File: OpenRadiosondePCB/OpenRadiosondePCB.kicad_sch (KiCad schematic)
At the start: 0 parts

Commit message: update
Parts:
- added IC1: SI4468-A2A-IMR, CustomLibs:QFN50P400X400X90-21N, symbol SI4468-A2A-IMR:SI4468-A2A-IMR
- added U1: STM32L476RGTx, Package_QFP:LQFP-64_10x10mm_P0.5mm, symbol MCU_ST_STM32L4:STM32L476RGTx
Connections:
- new net: U1.18 (VSS), U1.31 (VSS), U1.47 (VSS), U1.63 (VSS)

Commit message: Schematics inital work
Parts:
- added C1: 10u, symbol Device:C
- added C2, C3, C4, C5: 100n, symbol Device:C
- added C6, C7: C, symbol Device:C
- added J1: Conn_01x05, Connector_PinHeader_2.54mm:PinHeader_1x05_P2.54mm_Vertical, symbol Connector_Generic:Conn_01x05
- added Y1: Crystal_GND23, symbol Device:Crystal_GND23
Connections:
- net +3V3: now reaches U1.1 (VBAT)
- net +3V3: now also U1.19 (VDD), U1.32 (VDD), U1.64 (VDD), C1.1, C2.1, C3.1, C4.1, J1.1 (Pin_1)
- net GND: now reaches U1.12 (VSSA)
- net GND: now also U1.18 (VSS), U1.31 (VSS), U1.47 (VSS), U1.63 (VSS), C1.2, C2.2, C3.2, C4.2, C5.2, C6.2, C7.2, J1.5 (Pin_5), Y1.2 (G), Y1.3 (G)
- net at U1.46 (PA13): now also J1.2 (Pin_2)
- net at U1.49 (PA14): now also J1.3 (Pin_3)
- net RST: now reaches U1.7 (NRST)
- net RST: now also C5.1, J1.4 (Pin_4)
- new net HSE_IN: C6.1, Y1.1
- new net HSE_OUT: C7.1, Y1.4
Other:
- note added: "1 - VCC 2 - SWDIO 3 - SWCLK 4 - RST 5 - GND"

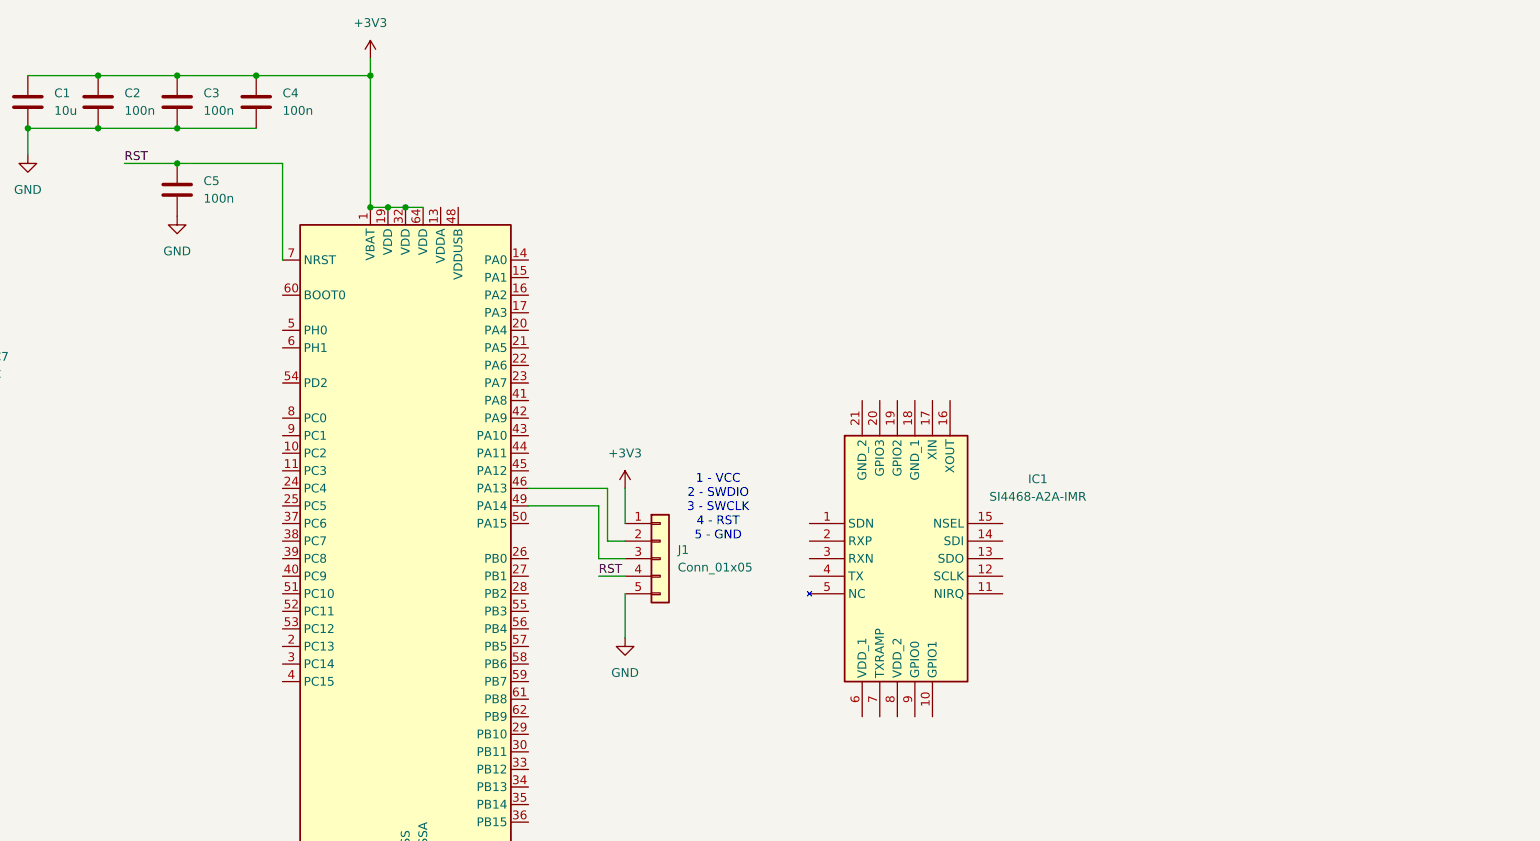
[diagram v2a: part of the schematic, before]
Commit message: Further PCB design and added CubeMX project
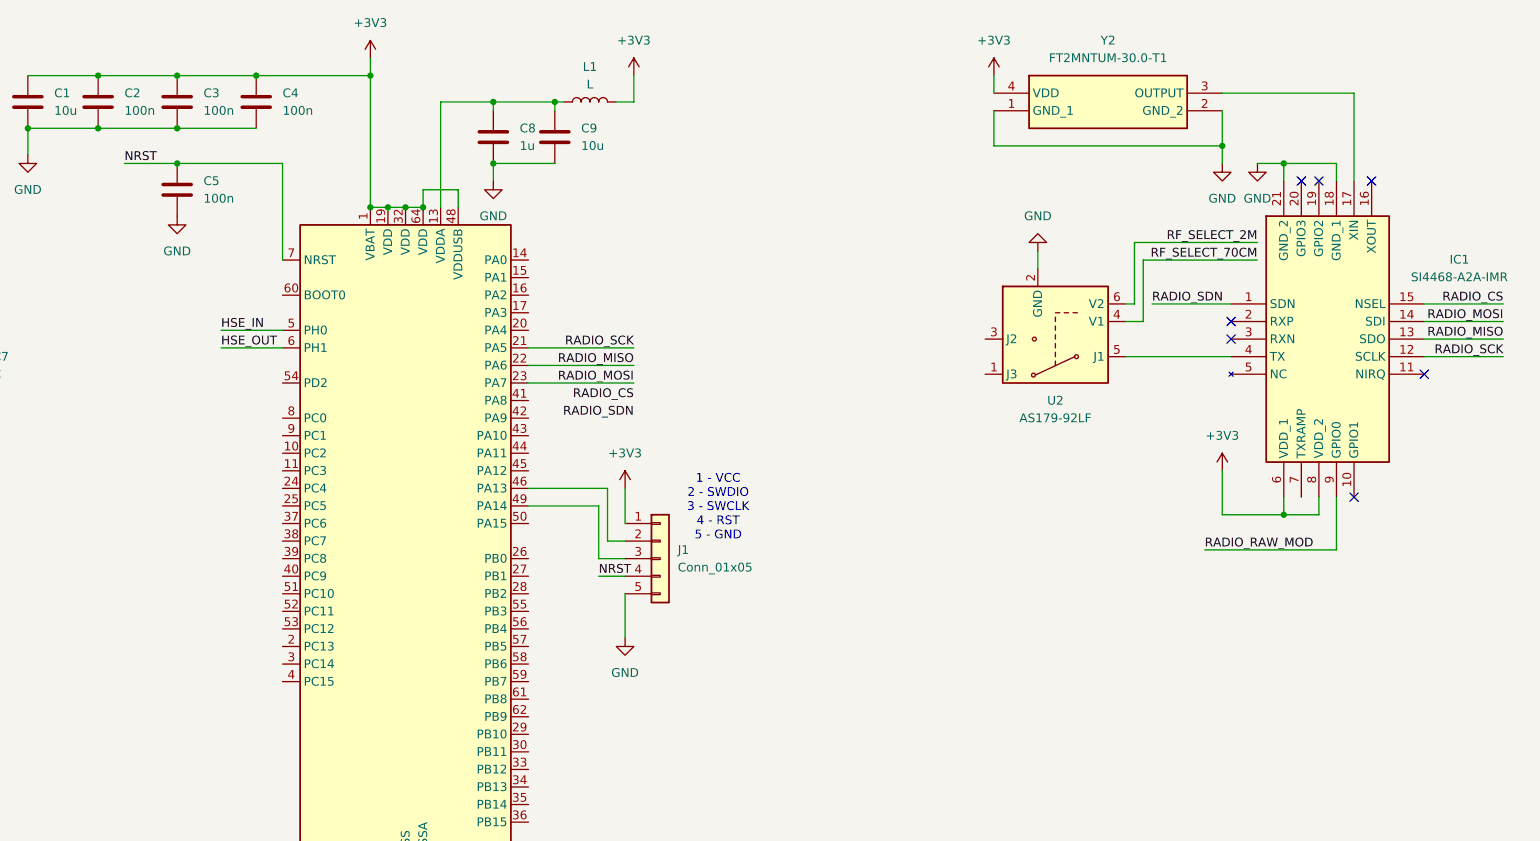
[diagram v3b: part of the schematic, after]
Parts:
- added C8: 1u, symbol Device:C
- added C9: 10u, symbol Device:C
- added L1: L, symbol Device:L
- added U2: AS179-92LF, Package_TO_SOT_SMD:SOT-363_SC-70-6, symbol RF_Switch:AS179-92LF
- added Y2: FT2MNTUM-30.0-T1, FT2MNTUM300T1, symbol FT2MNTUM-30_0-T1:FT2MNTUM-30.0-T1
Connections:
- net +3V3: now also IC1.6 (VDD_1), IC1.8 (VDD_2), U1.48 (VDDUSB), L1.2, Y2.4 (VDD)
- net GND: now also IC1.18 (GND_1), IC1.21 (GND_2), C8.2, C9.2, U2.2 (GND), Y2.1 (GND_1), Y2.2 (GND_2)
- net HSE_IN: now also U1.5 (PH0)
- net HSE_OUT: now also U1.6 (PH1)
- net RADIO_SDN: now reaches IC1.1 (SDN)
- net RADIO_SCK: now reaches IC1.12 (SCLK)
- net RADIO_SCK: now also U1.21 (PA5)
- net RADIO_MISO: now reaches IC1.13 (SDO)
- net RADIO_MISO: now also U1.22 (PA6)
- net RADIO_MOSI: now reaches IC1.14 (SDI)
- net RADIO_MOSI: now also U1.23 (PA7)
- net RADIO_CS: now reaches IC1.15 (NSEL)
- net at IC1.17 (XIN): now also Y2.3 (OUTPUT)
- net at IC1.4 (TX): now also U2.5 (J1)
- net RADIO_RAW_MOD: now reaches IC1.9 (GPIO0)
- net at U1.13 (VDDA): now also C8.1, C9.1, L1.1
- net RST renamed NRST
- new net RF_SELECT_2M: U2.6 (V2)
- new net RF_SELECT_70CM: U2.4 (V1)
- no-connect marks 0 -> 7
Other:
- moved on the sheet: IC1

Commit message: Further PCB work
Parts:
- removed Y1: Crystal_GND23, symbol Device:Crystal_GND23
- added C10: ???, symbol Device:C
- added C11: 100n, symbol Device:C
- added C12: C, symbol Device:C
- added C13: 1uF, symbol Device:C
- added C14: 10u, symbol Device:C
- added C15: 10n, symbol Device:C
- added C16: 13p, symbol Device:C
- added C17: 11p, symbol Device:C
- added C18: 22p, symbol Device:C
- added C19: 39p, symbol Device:C
- added C20: 33p, symbol Device:C
- added D2: ASMB-MTB0-0A3A2, LED_SMD:LED_Avago_PLCC4_3.2x2.8mm_CW, symbol LED:ASMB-MTB0-0A3A2
- added J2: GPS_ANT, symbol Connector:Conn_Coaxial
- added J3, J4: Conn_Coaxial_Small, symbol Connector:Conn_Coaxial_Small
- added L2: 2.2uH, Inductor_SMD:L_Coilcraft_LPS3010, symbol Device:L
- added L3: L, symbol Device:L
- added L4: 27nH, symbol Device:L
- added L5: 33nH, symbol Device:L
- added L6: 18nH, symbol Device:L
- added L7: 82nH, symbol Device:L
- added L8: 97nH, symbol Device:L
- added L9: 56nH, symbol Device:L
- added R1, R2, R3: 470R, symbol Device:R
- added R10, R11, R12: 1k, symbol Device:R
- added R13, R14: 22R, symbol Device:R
- added R4, R5: R, symbol Device:R
- added R6, R7: 4.7k, symbol Device:R
- added R8: 180k, symbol Device:R
- added R9: 1M, symbol Device:R
- added U3: MAX-M10S, RF_GPS:ublox_MAX, symbol RF_GPS:MAX-M10S
- added U4: TPS61202DRC, Package_SON:Texas_S-PVSON-N10_ThermalVias, symbol Regulator_Switching:TPS61202DRC
- C2: value 100n -> 10u
- C4: value 100n -> 1n
- C6: value C -> 1n
- C7: value C -> 7.5p
- L1: value L -> ???
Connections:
- net +3V3: now also D2.1 (A), L3.1, R6.1, R7.1, R9.1, U3.6 (V_BCKP), U3.7 (VCC_IO), U3.8 (VCC), U4.2 (VOUT); no longer Y2.4 (VDD)
- net GND: now also C11.2, C12.2, C13.1, C14.2, C15.2, C16.2, C17.2, C18.2, C19.2, C20.2, J2.2 (Ext), J3.2 (Ext), J4.2 (Ext), R5.2, R8.2, U3.1 (GND), U3.10 (GND), U3.12 (GND), U4.11 (PAD), U4.4 (PGND), U4.9 (GND); no longer C6.2
- net NRST: now also R10.1; no longer J1.4 (Pin_4)
- net RADIO_CS: now also U1.24 (PC4)
- net RADIO_RAW_MOD: now also U1.26 (PB0)
- net RADIO_SDN: now also U1.25 (PC5)
- net RF_SELECT_2M: now also U1.61 (PB8)
- net RF_SELECT_70CM: now also U1.62 (PB9)
- net at U2.1 (J3): now also C7.1, L4.1
- net at U2.3 (J2): now also C18.1, L7.1
- net at U2.5 (J1): now also C10.2; no longer IC1.4 (TX)
- net at IC1.17 (XIN): now also R14.1; no longer Y2.3 (OUTPUT)
- net at J1.2 (Pin_2): now also R12.2; no longer U1.46 (PA13)
- net at U1.49 (PA14): now also R11.1; no longer J1.3 (Pin_3)
- net GPS_PPS: now reaches U1.10 (PC2)
- net GPS_PPS: now also U3.4 (TIMEPULSE)
- net GPS_RESET: now reaches U1.11 (PC3)
- net GPS_RESET: now also U3.9 (~{RESET})
- net at U1.14 (PA0): now also C11.1, R4.1, R5.1
- net at U1.34 (PB13): now also R3.1
- net at U1.35 (PB14): now also R2.1
- net at U1.36 (PB15): now also R1.1
- net GPS_SCL: now reaches U1.58 (PB6)
- net GPS_SCL: now also R7.2, U3.16 (SDA)
- net GPS_SDA: now reaches U1.59 (PB7)
- net GPS_SDA: now also R6.2, U3.17 (SCL)
- net GPS_TX: now reaches U1.8 (PC0)
- net GPS_TX: now also U3.2 (TXD)
- net GPS_RX: now reaches U1.9 (PC1)
- net GPS_RX: now also U3.3 (RXD)
- net HSE_IN: no longer names the net of U1.5 (PH0)
- net HSE_IN: now also R13.2; no longer C6.1
- net HSE_OUT: no longer names the net of U1.6 (PH1)
- net HSE_OUT: no longer C7.1
- new net: C20.1, L8.2, L9.1
- new net: J4.1 (In), L9.2
- new net: C12.1, J2.1 (In), U3.11 (RF_IN)
- new net: C16.1, L4.2, L5.1
- new net: C17.1, L5.2, L6.1
- new net: D2.4 (RK), R3.2
- new net: J1.3 (Pin_3), R11.2
- new net: C13.2, U4.1 (VAUX)
- new net: C10.1, IC1.4 (TX)
- new net: R8.1, R9.2, U4.10 (FB)
- new net: C15.1, L3.2, Y2.4 (VDD)
- new net: J1.4 (Pin_4), R10.2
- new net: D2.2 (BK), R1.2
- new net: L2.2, U4.3 (L)
- new net: D2.3 (GK), R2.2
- new net: C19.1, L7.2, L8.1
- new net: C6.1, Y2.3 (OUTPUT)
- new net: R12.1, U1.46 (PA13)
- new net: J3.1 (In), L6.2
- new net +BATT: C14.1, L2.1, R4.2, U4.5 (VIN), U4.6 (EN), U4.7 (UVLO), U4.8 (PS)
- new net TCXO_OUT: C6.2, R13.1, R14.2
- no-connect marks 7 -> 14
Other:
- note added: "BAT ADC"
- note added: "BPF & ANT??"
- note added: "UART debug? sensor ports? cam connector? ADC?"
- moved on the sheet: C1, C2, C3, C4, C5, C8, C9, IC1, J1, L1, U1, U2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

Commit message: More PCB work
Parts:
- removed U4: TPS61202DRC, Package_SON:Texas_S-PVSON-N10_ThermalVias, symbol Regulator_Switching:TPS61202DRC
- added C21: 100pF, Capacitor_SMD:C_0402_1005Metric, symbol Device:C
- added C22: 220pF, Capacitor_SMD:C_0402_1005Metric, symbol Device:C
- added C23: 110pF, Capacitor_SMD:C_0402_1005Metric, symbol Device:C
- added L10: 100nH, Inductor_SMD:L_0402_1005Metric, symbol Device:L
- added R15: 180k, Resistor_SMD:R_0402_1005Metric, symbol Device:R
- added S1: PCM12SMTBR, CustomLibs:PCM12SMTBR, symbol CustomLibs:PCM12SMTBR
- added U5: TPS61201DRC, Package_SON:Texas_S-PVSON-N10_ThermalVias, symbol Regulator_Switching:TPS61201DRC
- C1, C14, C2, C9: value 10u -> 10uF; footprint (none) -> Capacitor_SMD:C_0402_1005Metric
- C10: value ??? -> 110pF; footprint (none) -> Capacitor_SMD:C_0402_1005Metric
- C11, C3, C5: value 100n -> 100nF; footprint (none) -> Capacitor_SMD:C_0402_1005Metric
- C12: value C -> ???; footprint (none) -> Capacitor_SMD:C_0402_1005Metric
- C13: footprint (none) -> Capacitor_SMD:C_0402_1005Metric
- C15: value 10n -> 10nF; footprint (none) -> Capacitor_SMD:C_0402_1005Metric
- C16: value 13p -> 13pF; footprint (none) -> Capacitor_SMD:C_0402_1005Metric
- C17: value 11p -> 11pF; footprint (none) -> Capacitor_SMD:C_0402_1005Metric
- C18: value 22p -> 22pF; footprint (none) -> Capacitor_SMD:C_0402_1005Metric
- C19: value 39p -> 39pF; footprint (none) -> Capacitor_SMD:C_0402_1005Metric
- C20: value 33p -> 33pF; footprint (none) -> Capacitor_SMD:C_0402_1005Metric
- C4, C6: value 1n -> 1nF; footprint (none) -> Capacitor_SMD:C_0402_1005Metric
- C7: value 7.5p -> 7.5pF; footprint (none) -> Capacitor_SMD:C_0402_1005Metric
- C8: value 1u -> 1uF; footprint (none) -> Capacitor_SMD:C_0402_1005Metric
- J2: footprint (none) -> Connector_Coaxial:U.FL_Hirose_U.FL-R-SMT-1_Vertical
- J3: value Conn_Coaxial_Small -> RF_OUT_70CM; footprint (none) -> Connector_Coaxial:SMA_Molex_73251-1153_EdgeMount_Horizontal
- J4: value Conn_Coaxial_Small -> RF_OUT_2M; footprint (none) -> Connector_Coaxial:SMA_Molex_73251-1153_EdgeMount_Horizontal
- L1, L4, L5, L6, L7, L9: footprint (none) -> Inductor_SMD:L_0402_1005Metric
- L2: footprint Inductor_SMD:L_Coilcraft_LPS3010 -> Inductor_SMD:L_0402_1005Metric
- L3: value L -> 100nH; footprint (none) -> Inductor_SMD:L_0402_1005Metric
- L8: value 97nH -> 91nH; footprint (none) -> Inductor_SMD:L_0402_1005Metric
- R1, R10, R11, R12, R13, R14, R2, R3, R6, R7, R8, R9: footprint (none) -> Resistor_SMD:R_0402_1005Metric
- R4: value R -> 100k; footprint (none) -> Resistor_SMD:R_0402_1005Metric
- R5: value R -> 150k; footprint (none) -> Resistor_SMD:R_0402_1005Metric
- Y2: footprint FT2MNTUM300T1 -> CustomLibs:FT2MNTUM300T1
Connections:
- net +3V3: now also C21.1, L10.1, U5.2 (VOUT)
- net +BATT: now also S1.3 (NO), U5.5 (VIN), U5.7 (UVLO), U5.8 (PS)
- net GND: now also C21.2, R15.2, U5.11 (PAD), U5.4 (PGND), U5.9 (GND)
- net at L9.2: now also C23.1; no longer J4.1 (In)
- net at C13.2: now also U5.1 (VAUX)
- net at C10.1, IC1.4 (TX): now also L10.2
- net at R8.1, R9.2: now also U5.10 (FB)
- net at L2.2: now also U5.3 (L)
- net at L6.2: now also C22.1; no longer J3.1 (In)
- new net: C23.2, J4.1 (In)
- new net: R15.1, S1.2 (COM), U5.6 (EN)
- new net: S1.MP1, S1.MP2, S1.MP3, S1.MP4
- new net: C22.2, J3.1 (In)
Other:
- moved on the sheet: C14, J3

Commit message: Added cammera, SRAM, LPS22 and more, changed MX project, more pin considerations, some schematics cleanup.
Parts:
- removed J1: Conn_01x05, Connector_PinHeader_2.54mm:PinHeader_1x05_P2.54mm_Vertical, symbol Connector_Generic:Conn_01x05
- added IC2: IS66WVS1M8BLL-104NLI, SOIC127P600X175-8N, symbol CustomLibs:IS66WVS1M8BLL-104NLI
- added J1: ICSP, symbol CustomLibs:ICSP
- added J5: SPI3, symbol CustomLibs:SPI3
- added J6: CAM, symbol CustomLibs:CAM
- added R16, R17, R20: 1k, symbol Device:R
- added R18: 180k, symbol Device:R
- added R19, R21, R22: 220R, symbol Device:R
- added U4: LPS22HB, Package_LGA:ST_HLGA-10_2x2mm_P0.5mm_LayoutBorder3x2y, symbol Sensor_Pressure:LPS22HB
- added U6: UART_DEBUG, Connector_PinHeader_2.54mm:PinHeader_1x03_P2.54mm_Vertical, symbol CustomLibs:UART_DEBUG
- C10, C23: value 110pF -> 220pF
- L1: value ??? -> 100nH
- R11, R12: value 1k -> 220R
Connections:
- net +3V3: now also IC2.8 (VDD), J1.1 (3.3V), J5.1 (3.3V), J6.1 (VCC), U4.1 (Vdd_IO), U4.10 (VDD)
- net GND: now also C5.1, IC2.4 (VSS), J1.5 (GND), J5.6 (GND), J6.2 (GND), U4.3 (GND), U4.8 (GND), U4.9 (GND), U6.1 (GND); no longer C5.2
- net GPS_PPS: no longer U1.10 (PC2)
- net GPS_RESET: no longer U1.11 (PC3)
- net NRST: now also C5.2; no longer C5.1
- net RADIO_CS: no longer U1.24 (PC4)
- net RADIO_RAW_MOD: no longer U1.26 (PB0)
- net RADIO_SDN: no longer U1.25 (PC5)
- net RF_SELECT_2M: now also R16.2; no longer U1.61 (PB8), U2.6 (V2)
- net RF_SELECT_70CM: now also R17.2; no longer U1.62 (PB9), U2.4 (V1)
- net CAM_SCL: now reaches U1.34 (PB13)
- net CAM_SCL: now also J6.3 (SCL); no longer R3.1
- net ICSP_SWCLK: now reaches R11.1, U1.49 (PA14)
- net at R11.2: now also J1.3 (SWCLK)
- net BAT_ADC: now reaches C11.1, R4.1, R5.1, U1.14 (PA0)
- net at S1.MP2, S1.MP3, S1.MP4: now also R18.1; no longer S1.MP1
- net at R10.2: now also J1.4 (RST)
- net at U1.36 (PB15): no longer R1.1
- net at R12.2: now also J1.2 (SWDIO)
- net LPS22_SCLK: now reaches U1.29 (PB10)
- net LPS22_SCLK: now also IC2.6 (CLK), U4.2 (SCL)
- net CAM_SDA: now reaches U1.30 (PB11)
- net CAM_SDA: now also J6.4 (SDA)
- net at U1.35 (PB14): no longer R2.1
- net DEBUG_TX: now reaches U1.42 (PA9)
- net DEBUG_TX: now also U6.2 (TX)
- net DEBUG_RX: now reaches U1.43 (PA10)
- net DEBUG_RX: now also U6.3 (RX)
- net ICSP_SWDIO: now reaches R12.1, U1.46 (PA13)
- net SPI3_SCK: now reaches U1.51 (PC10)
- net SPI3_MISO: now reaches U1.52 (PC11)
- net SPI3_MOSI: now reaches U1.53 (PC12)
- new net: J5.3 (SPI3_MISO), R21.2
- new net: R17.1, U2.4 (V1)
- new net: R16.1, U2.6 (V2)
- new net: R18.2, S1.MP1
- new net: J5.4 (SPI3_SCK), R22.2
- new net: J5.5 (SPI3_CS), R20.2
- new net: J5.2 (SPI3_MOSI), R19.2
- new net CAM_D0: J6.15 (D0)
- new net CAM_D1: J6.16 (D1)
- new net CAM_D2: J6.14 (D2)
- new net CAM_D3: J6.13 (D3)
- new net CAM_D4: J6.12 (D4)
- new net CAM_D5: J6.11 (D5)
- new net CAM_D6: J6.10 (D6)
- new net CAM_D7: J6.9 (D7)
- new net CAM_HREF: J6.6 (HS)
- new net CAM_PCLK: J6.7 (PCLK)
- new net CAM_PDN: J6.18 (PDN)
- new net CAM_RST: J6.17 (RST)
- new net CAM_VS: J6.5 (VS)
- new net CAM_XCLK: J6.8 (XCLK)
- new net LED_B: R1.1
- new net LED_G: R2.1
- new net LED_R: R3.1
- new net LPS22_CS: U4.6 (~{CS})
- new net LPS22_MISO: IC2.2 (SO/SIO1), U1.10 (PC2), U4.5 (SA0)
- new net LPS22_MOSI: IC2.5 (SI/SIO0), U1.11 (PC3), U4.4 (SDA)
- new net SPI3_OUT_CS: R20.1
- new net SPI3_OUT_MISO: R21.1
- new net SPI3_OUT_MOSI: R19.1
- new net SPI3_OUT_SCK: R22.1
- new net SRAM_CS: IC2.1 (CE#)
- no-connect marks 14 -> 15
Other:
- note removed: "1 - VCC 2 - SWDIO 3 - SWCLK 4 - RST 5 - GND"
- note removed: "BAT ADC"
- note removed: "BPF & ANT??"
- note removed: "UART debug? sensor ports? cam connector? ADC?"
- moved on the sheet: C1, C10, C11, C12, C13, C14, C15, C16, C17, C18, C19, C2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
